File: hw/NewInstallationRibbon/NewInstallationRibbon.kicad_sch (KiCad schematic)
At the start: 34 parts, among them J1 +5V, J10 D4, J11 8 Pin, J12 LEFT, J13 RIGHT, J14 UP, J15 GND, J16 GND, J17 20 Pin, J18 DOWN, J19 R, J2 GND, J20 L, J21 START, J22 B_1, J23 B_2, J25 BRIGHT, J3 CLK, J4 SMS, J5 DW, J6 CL2, J7 D1, J8 D2, J9 D3

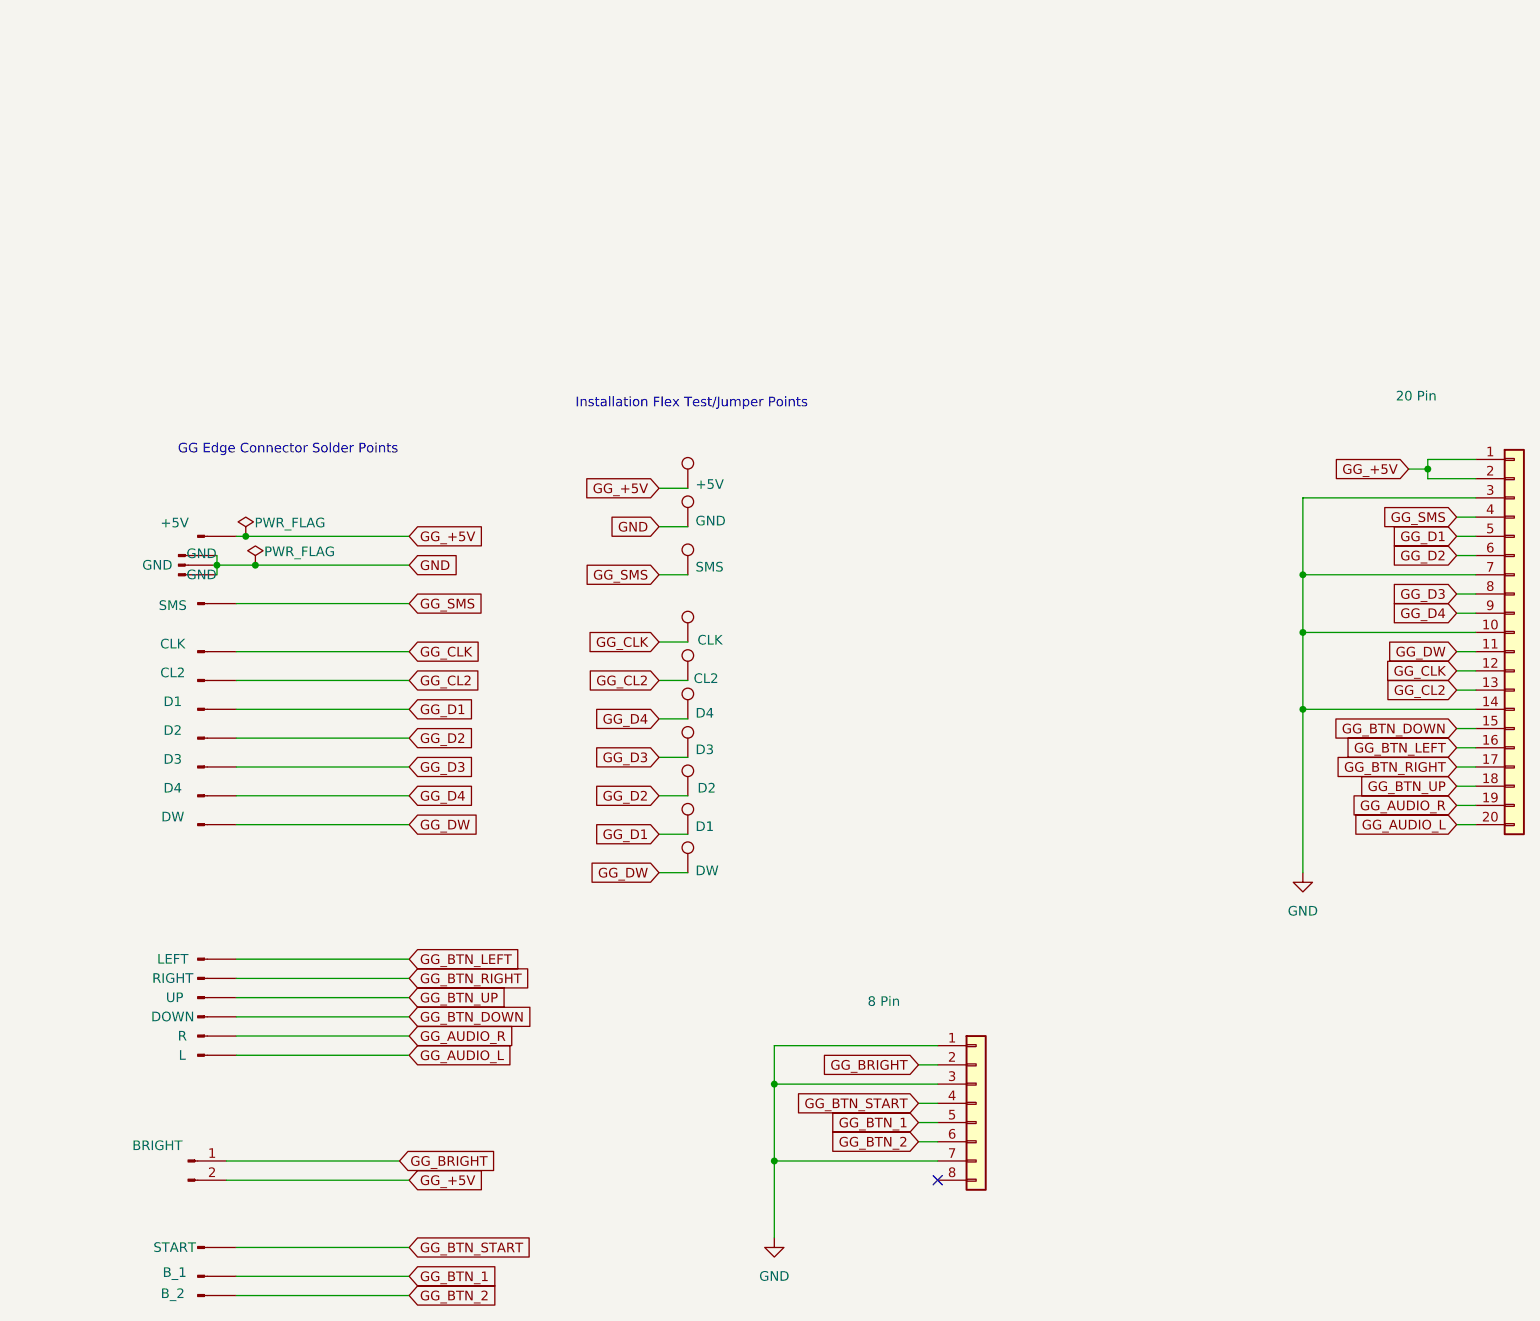
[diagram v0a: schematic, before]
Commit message: Added LM358 op-amp for both audio channels.
Updated ribbon connector pin assignments, text labels, and tweaked board outline.
Gerbers updated for production.
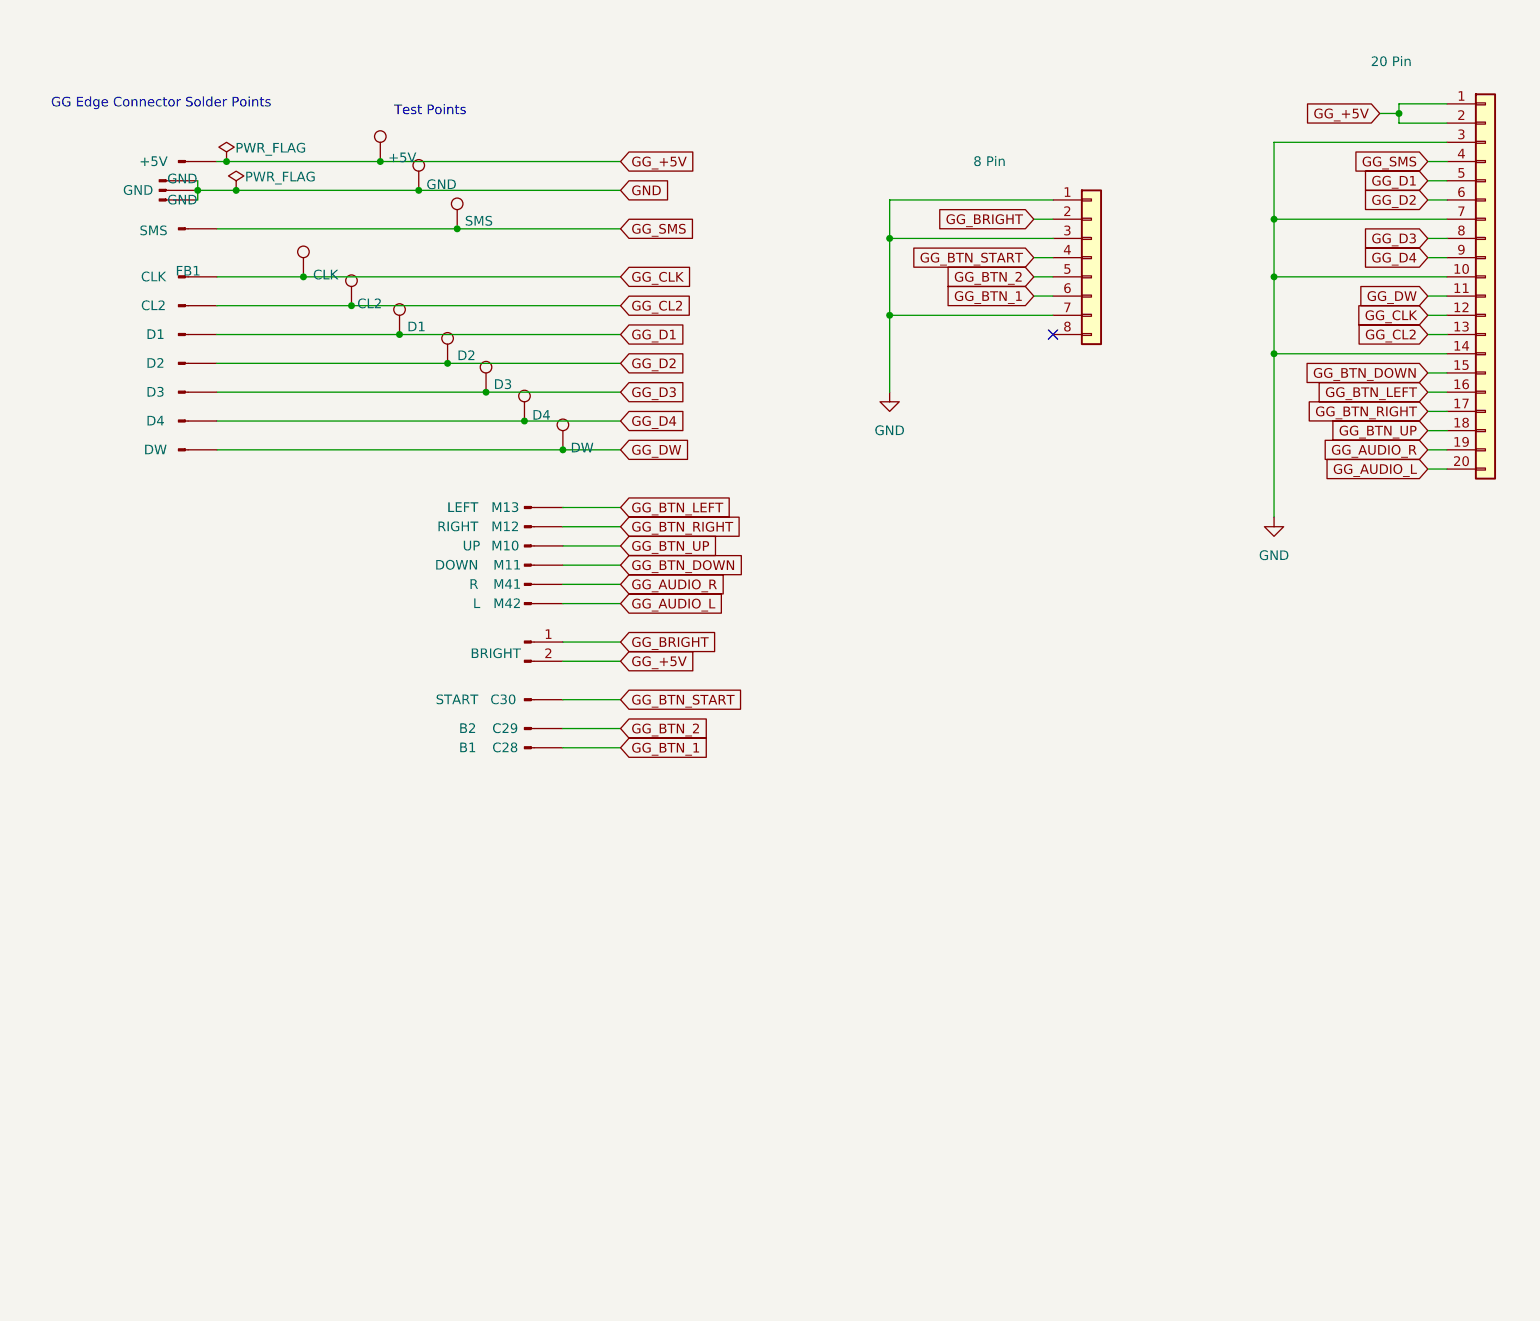
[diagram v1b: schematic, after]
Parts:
- J1, J15, J16, J2, J4: footprint gg_lcd:TestPoint_THTPad_D2.5mm_Drill1.2mm_OneSided -> gg_lcd:TestPoint_THTPad_D2.5mm_Drill1.2mm
- J12: footprint gg_lcd:TestPoint_THTPad_D2.5mm_Drill1.2mm_OneSided -> gg_lcd:TestPoint_THTPad_D2.5mm_Drill1.2mm; Ref2 (none) -> M13
- J13: footprint gg_lcd:TestPoint_THTPad_D2.5mm_Drill1.2mm_OneSided -> gg_lcd:TestPoint_THTPad_D2.5mm_Drill1.2mm; Ref2 (none) -> M12
- J14: footprint gg_lcd:TestPoint_THTPad_D2.5mm_Drill1.2mm_OneSided -> gg_lcd:TestPoint_THTPad_D2.5mm_Drill1.2mm; Ref2 (none) -> M10
- J18: footprint gg_lcd:TestPoint_THTPad_D2.5mm_Drill1.2mm_OneSided -> gg_lcd:TestPoint_THTPad_D2.5mm_Drill1.2mm; Ref2 (none) -> M11
- J19: footprint gg_lcd:TestPoint_THTPad_D2.5mm_Drill1.2mm_OneSided -> gg_lcd:TestPoint_THTPad_D2.5mm_Drill1.2mm; Ref2 (none) -> M41
- J20: footprint gg_lcd:TestPoint_THTPad_D2.5mm_Drill1.2mm_OneSided -> gg_lcd:TestPoint_THTPad_D2.5mm_Drill1.2mm; Ref2 (none) -> M42
- J21: footprint gg_lcd:TestPoint_THTPad_D2.5mm_Drill1.2mm_OneSided -> gg_lcd:TestPoint_THTPad_D2.5mm_Drill1.2mm; Ref2 (none) -> C30
- J22: value B_1 -> B2; footprint gg_lcd:TestPoint_THTPad_D2.5mm_Drill1.2mm_OneSided -> gg_lcd:TestPoint_THTPad_D2.5mm_Drill1.2mm; Ref2 (none) -> C29
- J23: value B_2 -> B1; footprint gg_lcd:TestPoint_THTPad_D2.5mm_Drill1.2mm_OneSided -> gg_lcd:TestPoint_THTPad_D2.5mm_Drill1.2mm; Ref2 (none) -> C28
- J3: footprint gg_lcd:TestPoint_THTPad_D2.5mm_Drill1.2mm_OneSided -> gg_lcd:TestPoint_THTPad_D2.5mm_Drill1.2mm; Ref2 (none) -> FB1
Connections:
- net GG_BTN_1: now also J11.6 (Pin_6), J23.1 (Pin_1); no longer J11.5 (Pin_5), J22.1 (Pin_1)
- net GG_BTN_2: now also J11.5 (Pin_5), J22.1 (Pin_1); no longer J11.6 (Pin_6), J23.1 (Pin_1)
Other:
- note added: "Test Points"
- note removed: "Installation Flex Test/Jumper Points"

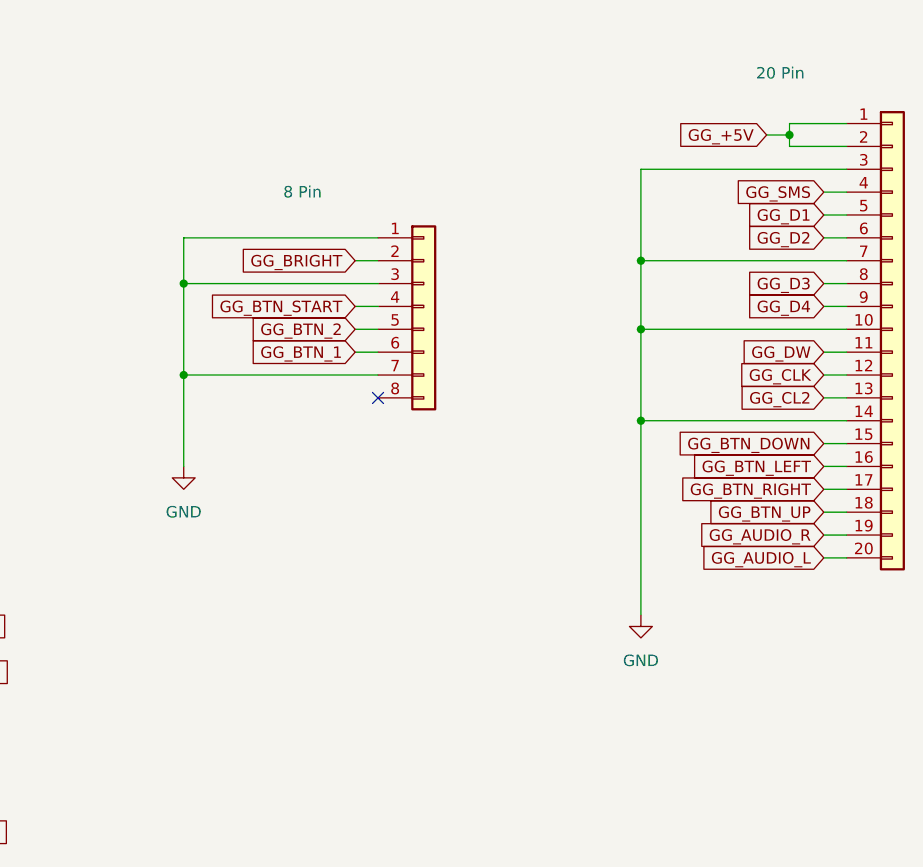
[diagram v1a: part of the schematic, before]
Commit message: Flex PCB updated:
- Use a single 24pin connection to the main board, pin out updated to match the main board.
- Various layout tweaks to improve installation by reducing some of the slack.
- Added rule areas around solder points to exclude copper fills to help align the solder points.
- Added guide holes for the top row of cartridge connector pins, and tweaked the other guide holes to help with install.
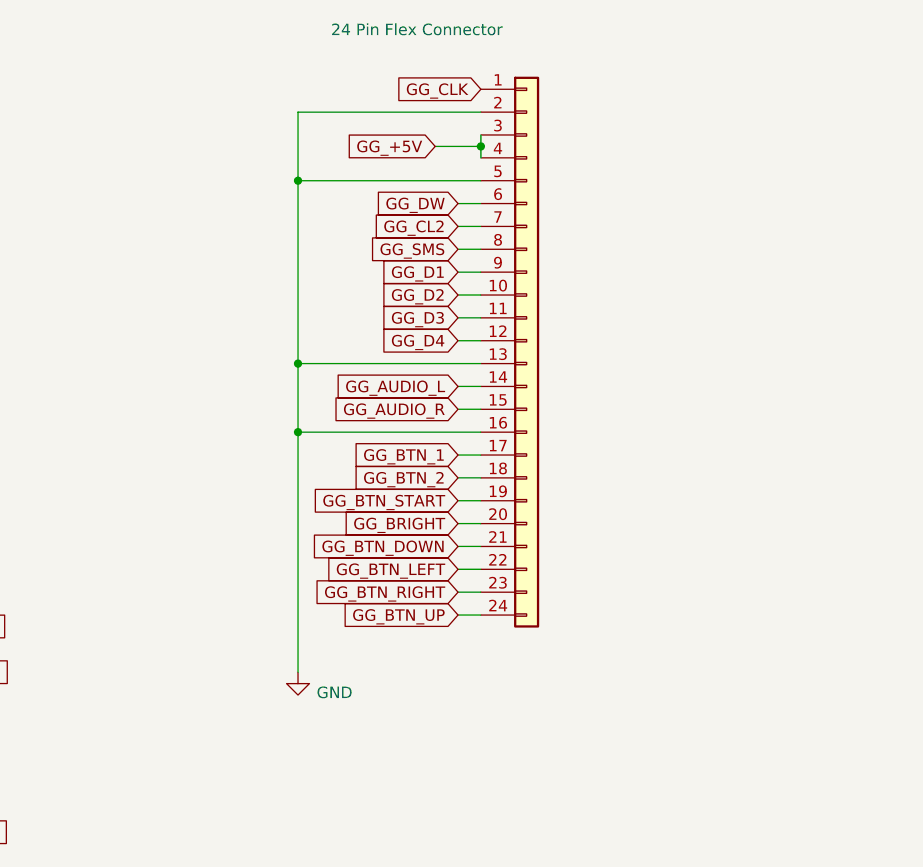
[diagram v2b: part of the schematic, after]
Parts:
- removed J11: 8 Pin, gg_lcd:Flex Connector 0.5mm 01x08Pin, symbol Connector_Generic:Conn_01x08
- J17: value 20 Pin -> 24 Pin Flex Connector; footprint gg_lcd:Flex Connector 0.5mm 01x20Pin -> gg_lcd:Flex Connector 0.5mm 01x24Pin; symbol Connector_Generic:Conn_01x20 -> Connector_Generic:Conn_01x24; now in the parts list
- J21, J22, J23, J3: footprint gg_lcd:TestPoint_THTPad_D2.5mm_Drill1.2mm -> gg_lcd:TestPoint_THTPad_D2.5x2.5mm_Drill1.2mm; now in the parts list
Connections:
- net GG_+5V: now also J17.3 (Pin_3), J17.4 (Pin_4); no longer J17.1 (Pin_1), J17.2 (Pin_2)
- net GG_AUDIO_L: now also J17.14 (Pin_14); no longer J17.20 (Pin_20)
- net GG_AUDIO_R: now also J17.15 (Pin_15); no longer J17.19 (Pin_19)
- net GG_BRIGHT: now also J17.20 (Pin_20)
- net GG_BTN_1: now also J17.17 (Pin_17)
- net GG_BTN_2: now also J17.18 (Pin_18)
- net GG_BTN_DOWN: now also J17.21 (Pin_21); no longer J17.15 (Pin_15)
- net GG_BTN_LEFT: now also J17.22 (Pin_22); no longer J17.16 (Pin_16)
- net GG_BTN_RIGHT: now also J17.23 (Pin_23); no longer J17.17 (Pin_17)
- net GG_BTN_START: now also J17.19 (Pin_19)
- net GG_BTN_UP: now also J17.24 (Pin_24); no longer J17.18 (Pin_18)
- net GG_CL2: now also J17.7 (Pin_7); no longer J17.13 (Pin_13)
- net GG_CLK: now also J17.1 (Pin_1); no longer J17.12 (Pin_12)
- net GG_D1: now also J17.9 (Pin_9); no longer J17.5 (Pin_5)
- net GG_D2: now also J17.10 (Pin_10); no longer J17.6 (Pin_6)
- net GG_D3: now also J17.11 (Pin_11); no longer J17.8 (Pin_8)
- net GG_D4: now also J17.12 (Pin_12); no longer J17.9 (Pin_9)
- net GG_DW: now also J17.6 (Pin_6); no longer J17.11 (Pin_11)
- net GG_SMS: now also J17.8 (Pin_8); no longer J17.4 (Pin_4)
- net GND: now also J17.13 (Pin_13), J17.16 (Pin_16), J17.2 (Pin_2), J17.5 (Pin_5); no longer J17.10 (Pin_10), J17.14 (Pin_14), J17.3 (Pin_3), J17.7 (Pin_7)
- no-connect marks 1 -> 0

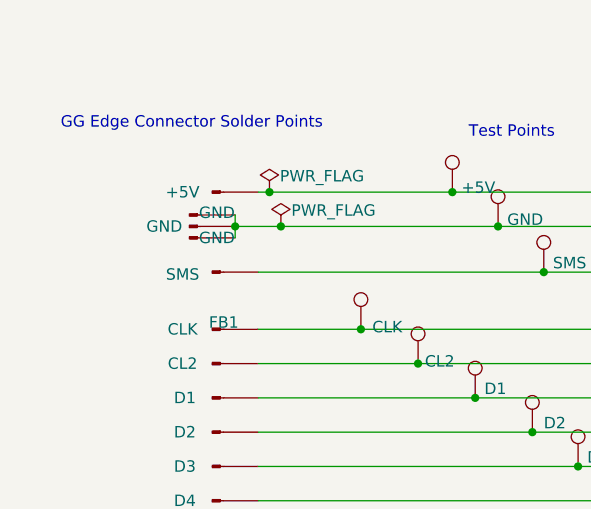
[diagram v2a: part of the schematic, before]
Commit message: Fixed wrong GND pin on installation ribbon!
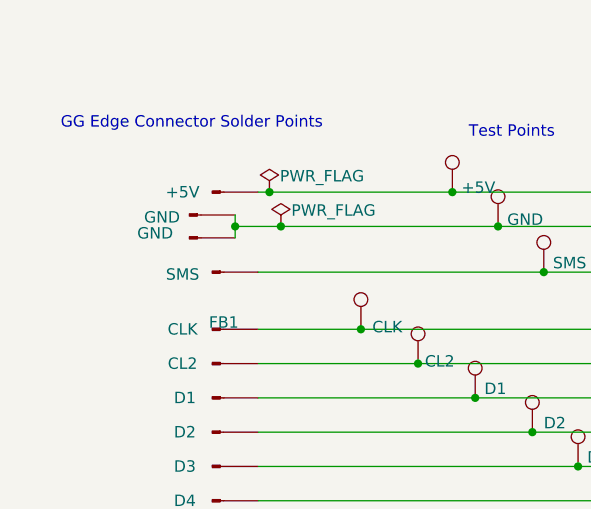
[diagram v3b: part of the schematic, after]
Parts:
- removed J2: GND, gg_lcd:TestPoint_THTPad_D2.5mm_Drill1.2mm, symbol Connector:Conn_01x01_Pin
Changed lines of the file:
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@@
 		)
 		(property "Value" "GND"
-			(at 52.578 44.45 0)
+			(at 45.72 43.942 0)
 			(effects
 				(font
@@
 		)
 		(property "Value" "GND"
-			(at 52.578 41.656 0)
+			(at 46.482 42.164 0)
 			(effects
 				(font
@@
 					(unit 1)
 				)
-			)
-		)
-	)
-	(symbol
-		(lib_id "Connector:Conn_01x01_Pin")
-		(at 49.53 43.18 0)
-		(unit 1)
-		(exclude_from_sim no)
-		(in_bom no)
-		(on_board yes)
-		(dnp no)
-		(property "Reference" "J2"
-			(at 51.816 41.656 0)
-			(effects
-				(font
-					(size 1.27 1.27)
-				)
-				(hide yes)
-			)
-		)
-		(property "Value" "GND"
-			(at 46.736 43.18 0)
-			(effects
-				(font
-					(size 1.27 1.27)
-				)
-			)
-		)
-		(property "Footprint" "gg_lcd:TestPoint_THTPad_D2.5mm_Drill1.2mm"
-			(at 49.53 43.18 0)
-			(effects
-				(font
-					(size 1.27 1.27)
-				)
-				(hide yes)
-			)
-		)
-		(property "Datasheet" "~"
-			(at 49.53 43.18 0)
-			(effects
-				(font
-					(size 1.27 1.27)
-				)
-				(hide yes)
-			)
-		)
-		(property "Description" "Generic connector, single row, 01x01, script generated"
-			(at 49.53 43.18 0)
-			(effects
-				(font
-					(size 1.27 1.27)
-				)
-				(hide yes)
-			)
-		)
-		(pin "1"
-		)
-		(instances
-			(project "InstallationFlex"
-				(path "/a76be214-be29-4d5c-b6c1-be579b0fd0f5"
-					(reference "J2")
-					(unit 1)
-				)
